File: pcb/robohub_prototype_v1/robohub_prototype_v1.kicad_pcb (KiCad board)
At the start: 10 copper layers, 102 parts, among them J21 Barrel_Jack_Switch_Pin3Ring, J51 USB_A, J52 USB_A, J71 USB_A, U1 ATSAMA5D27C, U21 LM3880, U22 TPS564242DRL, U23 TPS564242DRL, U24 TPS564242DRL, U25 TPS564242DRL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

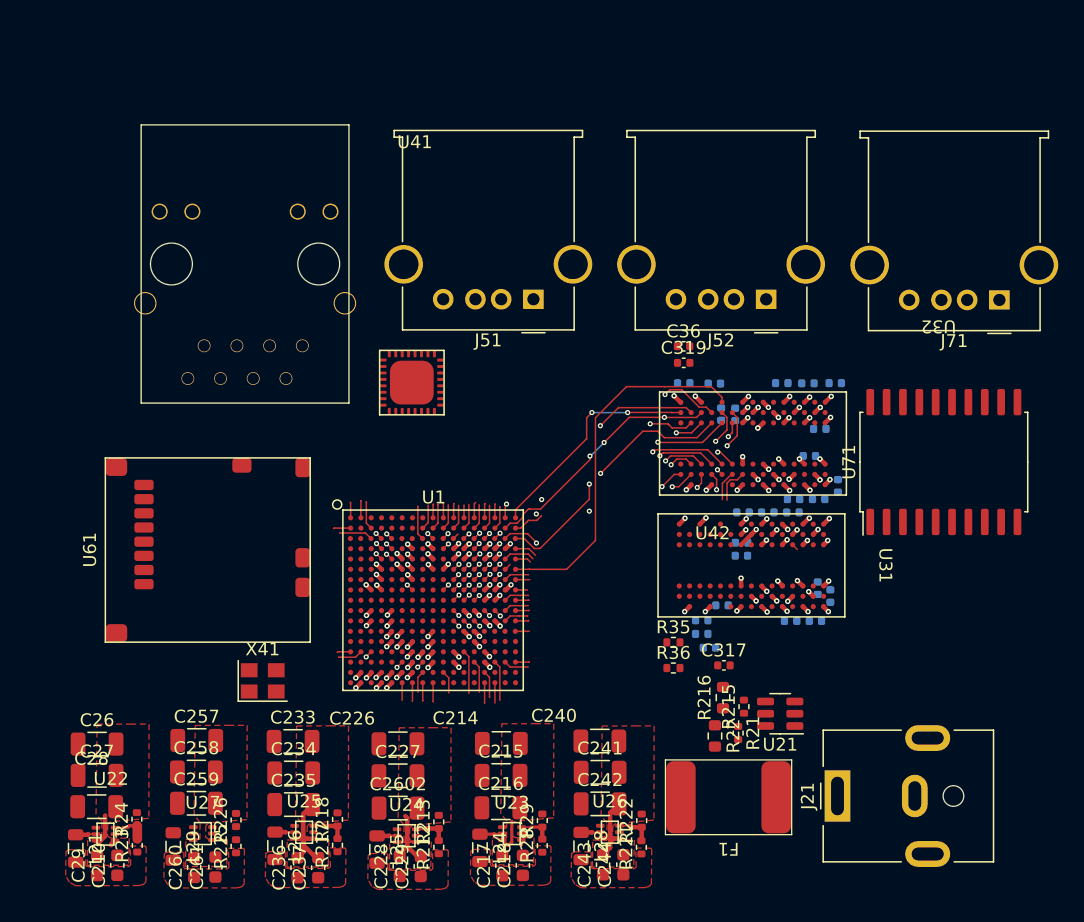
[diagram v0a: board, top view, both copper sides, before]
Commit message: Update schematic for byte swap; change ddr2 layout; begin reroute of ddr2
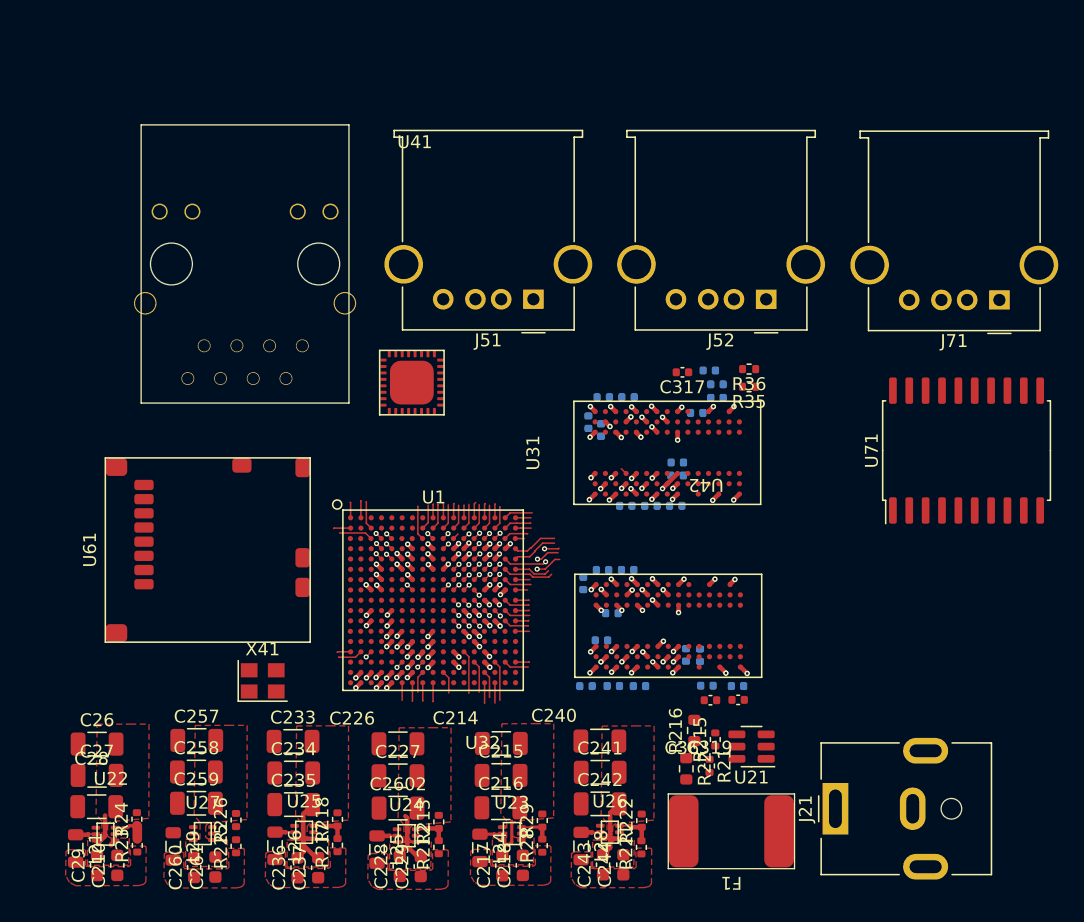
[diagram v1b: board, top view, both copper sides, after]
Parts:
- moved C314 30.4 mm to (133.7, 101.4), turned to 180 degrees
- moved C315 27.9 mm to (135.8, 101.4), turned to 0 degrees
- moved C36 27.5 mm to (143.4, 102.5), turned to 180 degrees
- moved C319 26.5 mm to (145.5, 102.5), turned to 180 degrees
- moved C316 26.0 mm to (137.9, 101.4), turned to 180 degrees
- moved C321 23.9 mm to (135.1, 79.0), turned to 0 degrees
- moved R36 23.9 mm to (146.4, 76.8), turned to 180 degrees
- moved C318 23.9 mm to (145.5, 101.4), turned to 180 degrees
- moved C311 23.6 mm to (134.9, 97.8), turned to 180 degrees
- moved C35 23.5 mm to (143.1, 101.3), turned to 0 degrees
- moved C327 23.1 mm to (133.9, 80.9), turned to -90 degrees
- moved C317 23.0 mm to (141.2, 77.0), turned to 180 degrees
- moved C37 21.5 mm to (143.3, 76.9), turned to 180 degrees
- moved C326 21.5 mm to (137.0, 79.0), turned to 180 degrees
- moved C322 21.2 mm to (133.5, 93.4), turned to 90 degrees
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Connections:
- net VCC_3_3_A renamed VDDBU
- U31 pad A8: /DDR2_3/DDR_DQS1- -> /DDR2_3/DDR_DQS2-
- U31 pad B1: /DDR2_3/DDR_D14 -> /DDR2_3/DDR_D22
- U31 pad B3: /DDR2_3/DDR_DQM1 -> /DDR2_3/DDR_DQM2
- U31 pad B7: /DDR2_3/DDR_DQS1+ -> /DDR2_3/DDR_DQS2+
- U31 pad B9: /DDR2_3/DDR_D15 -> /DDR2_3/DDR_D23
- U31 pad C2: /DDR2_3/DDR_D9 -> /DDR2_3/DDR_D17
- U31 pad C8: /DDR2_3/DDR_D8 -> /DDR2_3/DDR_D16
- U31 pad D1: /DDR2_3/DDR_D12 -> /DDR2_3/DDR_D20
- U31 pad D3: /DDR2_3/DDR_D11 -> /DDR2_3/DDR_D19
- U31 pad D7: /DDR2_3/DDR_D10 -> /DDR2_3/DDR_D18
- U31 pad D9: /DDR2_3/DDR_D13 -> /DDR2_3/DDR_D21
- U32 pad E8: /DDR2_3/DDR_DQS2- -> /DDR2_3/DDR_DQS1-
- U32 pad F1: /DDR2_3/DDR_D22 -> /DDR2_3/DDR_D14
- U32 pad F3: /DDR2_3/DDR_DQM2 -> /DDR2_3/DDR_DQM1
- U32 pad F7: /DDR2_3/DDR_DQS2+ -> /DDR2_3/DDR_DQS1+
- U32 pad F9: /DDR2_3/DDR_D23 -> /DDR2_3/DDR_D15
- U32 pad G2: /DDR2_3/DDR_D17 -> /DDR2_3/DDR_D9
- U32 pad G8: /DDR2_3/DDR_D16 -> /DDR2_3/DDR_D8
- U32 pad H1: /DDR2_3/DDR_D20 -> /DDR2_3/DDR_D12
- U32 pad H3: /DDR2_3/DDR_D19 -> /DDR2_3/DDR_D11
- U32 pad H7: /DDR2_3/DDR_D18 -> /DDR2_3/DDR_D10
- U32 pad H9: /DDR2_3/DDR_D21 -> /DDR2_3/DDR_D13
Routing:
- net /DDR2_3/DDR_BA2: track 28.2 -> 2.82 mm
- net /DDR2_3/DDR_RAS: track 26.7 -> 6.35 mm, vias 3 -> 1
- net /DDR2_3/DDR_CS: track 26.4 -> 6.37 mm, vias 2 -> 1
- net /DDR2_3/DDR_A1: track 20.7 -> 0.70 mm, vias 2 -> 0
- net /DDR2_3/DDR_A10: track 22.4 -> 3.55 mm, vias 2 -> 1
- net /DDR2_3/DDR_A5: track 23.5 -> 5.43 mm, vias 2 -> 1
- net /DDR2_3/DDR_A4: track 20.0 -> 1.91 mm, vias 2 -> 0
- net /DDR2_3/DDR_A0: track 25.1 -> 7.89 mm
- net /DDR2_3/DDR_A3: track 19.2 -> 2.14 mm, vias 3 -> 0
- net /DDR2_3/DDR_A12: track 17.6 -> 1.19 mm, vias 2 -> 0
- net /DDR2_3/DDR_A8: track 21.0 -> 4.72 mm, vias 2 -> 1
- net /DDR2_3/DDR_A7: track 25.5 -> 9.23 mm
- net /DDR2_3/DDR_A11: track 18.2 -> 2.25 mm, vias 4 -> 0
- net /DDR2_3/DDR_A9: track 21.2 -> 5.41 mm, vias 2 -> 1
- net /DDR2_3/DDR_A13: track 23.3 -> 8.91 mm
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
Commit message: Moved some stuff around, tried a route
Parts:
- moved C310 5.03 mm to (133.7, 87.1)
- moved C312 5.03 mm to (131.8, 87.1)
- moved C320 5.03 mm to (138.9, 78.7)
- moved C331 5.03 mm to (135.8, 83.7)
- moved C37 5.03 mm to (138.3, 76.6)
- moved C39 5.03 mm to (135.7, 87.1)
- moved R35 5.03 mm to (141.3, 77.8)
- moved R36 5.03 mm to (141.3, 76.5)
- moved U31 5.03 mm to (135.0, 83.0)
- moved C321 5.03 mm to (130.0, 78.7)
- moved C325 5.03 mm to (129.9, 81.2)
- moved C327 5.03 mm to (128.9, 80.6)
- moved C328 5.03 mm to (137.3, 79.9)
- moved C330 5.03 mm to (135.8, 84.7)
- moved C38 5.03 mm to (138.9, 77.7)
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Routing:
- net /DDR2_3/DDR_A12: track 1.19 -> 15.9 mm
- net /DDR2_3/DDR_A7: track 9.23 -> 0.90 mm, vias 2 -> 1
- net /DDR2_3/DDR_A13: track 8.91 -> 0.57 mm, vias 2 -> 1
- net /DDR2_3/DDR_A0: track 7.89 -> 0.58 mm, vias 2 -> 1
- net /DDR2_3/DDR_CKE: track 3.94 -> 0.00 mm
- net /DDR2_3/DDR_CLK+: track 3.57 -> 0.00 mm
- net /DDR2_3/DDR_CLK-: track 3.58 -> 0.15 mm
- net /DDR2_3/DDR_BA2: track 2.82 -> 0.01 mm
- net /DDR2_3/DDR_A11: track 2.25 -> 0.00 mm
- net /DDR2_3/DDR_A3: track 2.14 -> 0.67 mm
- net /DDR2_3/DDR_A2: track 1.21 -> 0.00 mm
- net Net-(U1E-DDR_RESETN): track 3.37 -> 2.81 mm, vias 1 -> 0
- net VCC_1_8_DDR: vias 39 -> 38

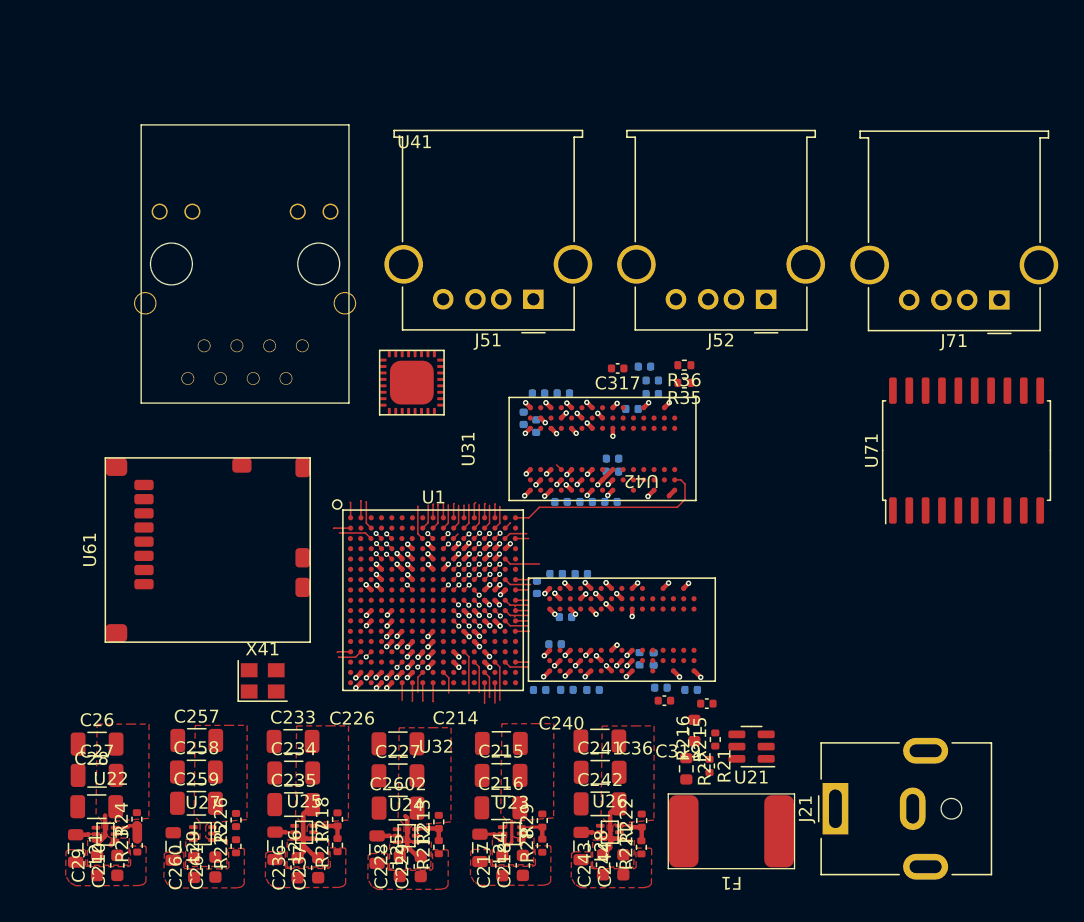
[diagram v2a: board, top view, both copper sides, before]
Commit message: Update PCB route to match example design
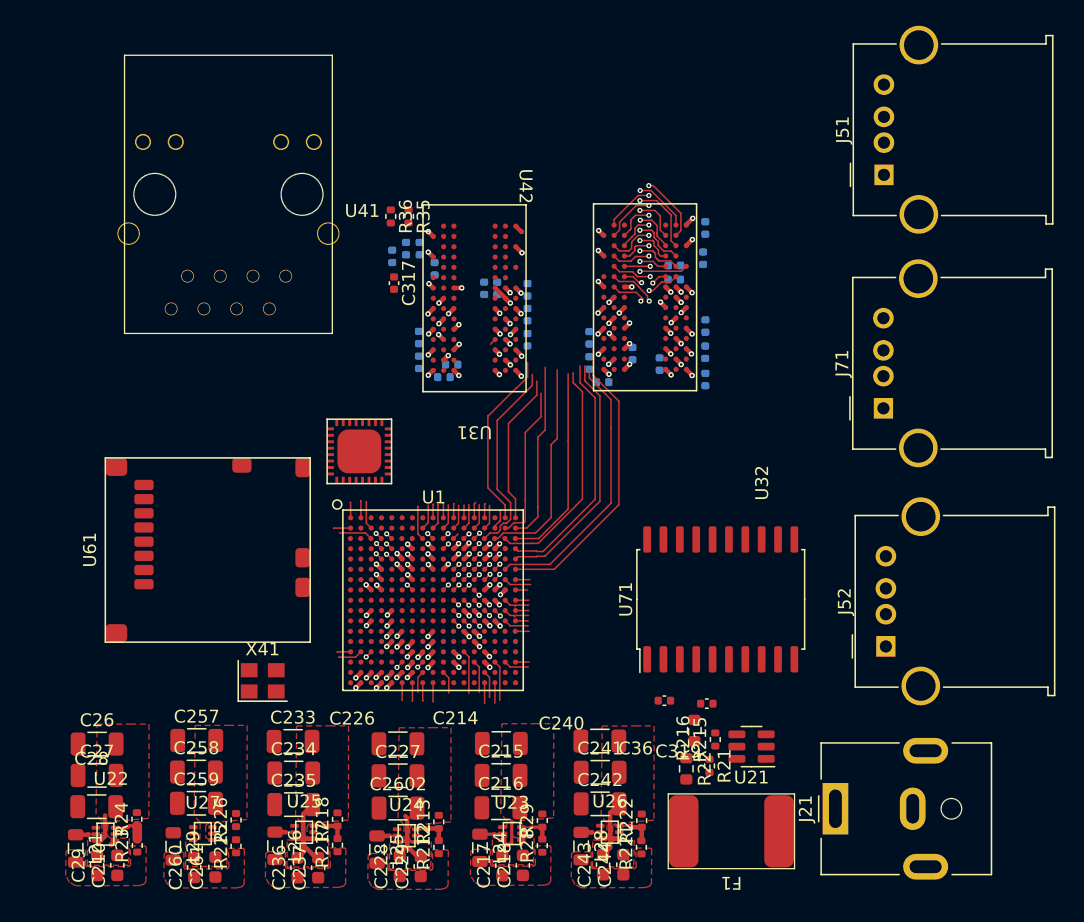
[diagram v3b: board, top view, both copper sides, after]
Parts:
- moved C318 35.9 mm to (143.0, 65.8), turned to -90 degrees
- moved C35 33.5 mm to (142.8, 68.2), turned to 90 degrees
- moved C34 30.6 mm to (140.6, 68.7), turned to 180 degrees
- moved C316 29.6 mm to (143.0, 73.4), turned to -90 degrees
- moved C33 29.6 mm to (140.6, 69.8), turned to 180 degrees
- moved J51 28.9 mm to (156.8, 61.7), turned to 90 degrees
- moved J52 28.5 mm to (157.0, 98.3), turned to 90 degrees
- moved C315 28.3 mm to (143.0, 75.5), turned to 90 degrees
- moved C314 27.3 mm to (143.0, 77.6), turned to -90 degrees
- moved U32 25.9 mm to (138.3, 71.2), turned to 180 degrees
- moved R36 25.5 mm to (118.6, 64.9), turned to -90 degrees
- moved R35 25.0 mm to (119.9, 64.9), turned to -90 degrees
- moved C311 23.2 mm to (139.4, 76.4), turned to -90 degrees
- moved U71 22.3 mm to (144.2, 94.7)
- moved C38 21.7 mm to (119.8, 67.4), turned to 90 degrees
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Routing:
- net /DDR2_3/DDR_BA2: track 0.01 -> 26.8 mm, vias 0 -> 1
- net /DDR2_3/DDR_CKE: track 0.00 -> 23.9 mm, vias 0 -> 1
- net /DDR2_3/DDR_CLK-: track 0.15 -> 22.6 mm, vias 0 -> 1
- net /DDR2_3/DDR_CLK+: track 0.00 -> 22.2 mm, vias 0 -> 1
- net /DDR2_3/DDR_A10: track 3.55 -> 23.7 mm
- net /DDR2_3/DDR_A4: track 1.86 -> 21.4 mm, vias 0 -> 1
- net /DDR2_3/DDR_A8: track 4.72 -> 23.8 mm
- net /DDR2_3/DDR_A1: track 1.07 -> 18.4 mm, vias 0 -> 1
- net /DDR2_3/DDR_A3: track 0.67 -> 17.7 mm, vias 0 -> 1
- net /DDR2_3/DDR_A11: track 0.00 -> 16.9 mm, vias 0 -> 1
- net /DDR2_3/DDR_A2: track 0.00 -> 16.3 mm, vias 0 -> 1
- net /DDR2_3/DDR_A7: track 0.90 -> 6.15 mm, vias 1 -> 2
- net /DDR2_3/DDR_A13: track 0.57 -> 4.48 mm, vias 1 -> 2
- net /DDR2_3/DDR_BA0: track 7.08 -> 10.6 mm, vias 1 -> 2
- net /DDR2_3/DDR_A9: track 5.41 -> 8.86 mm, vias 1 -> 2
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
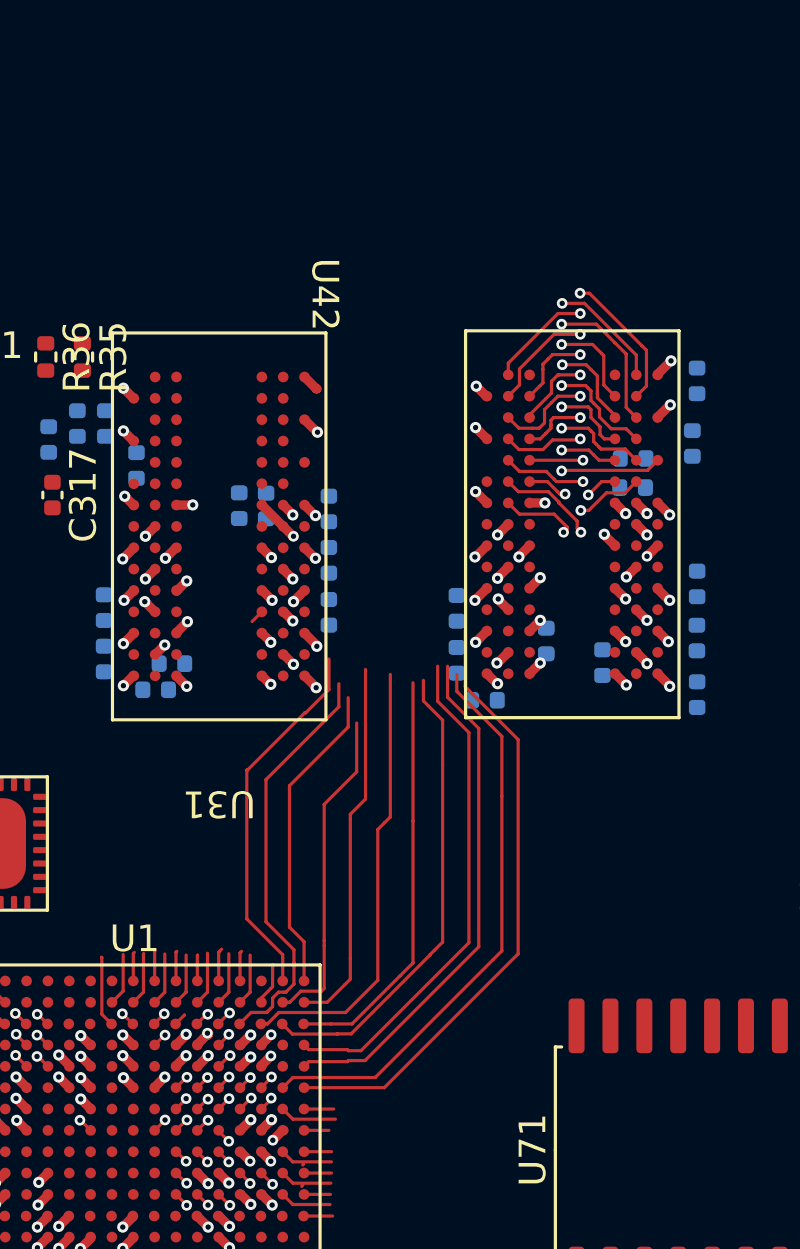
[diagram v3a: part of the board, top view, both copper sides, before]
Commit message: Update PCB routing of DDR2
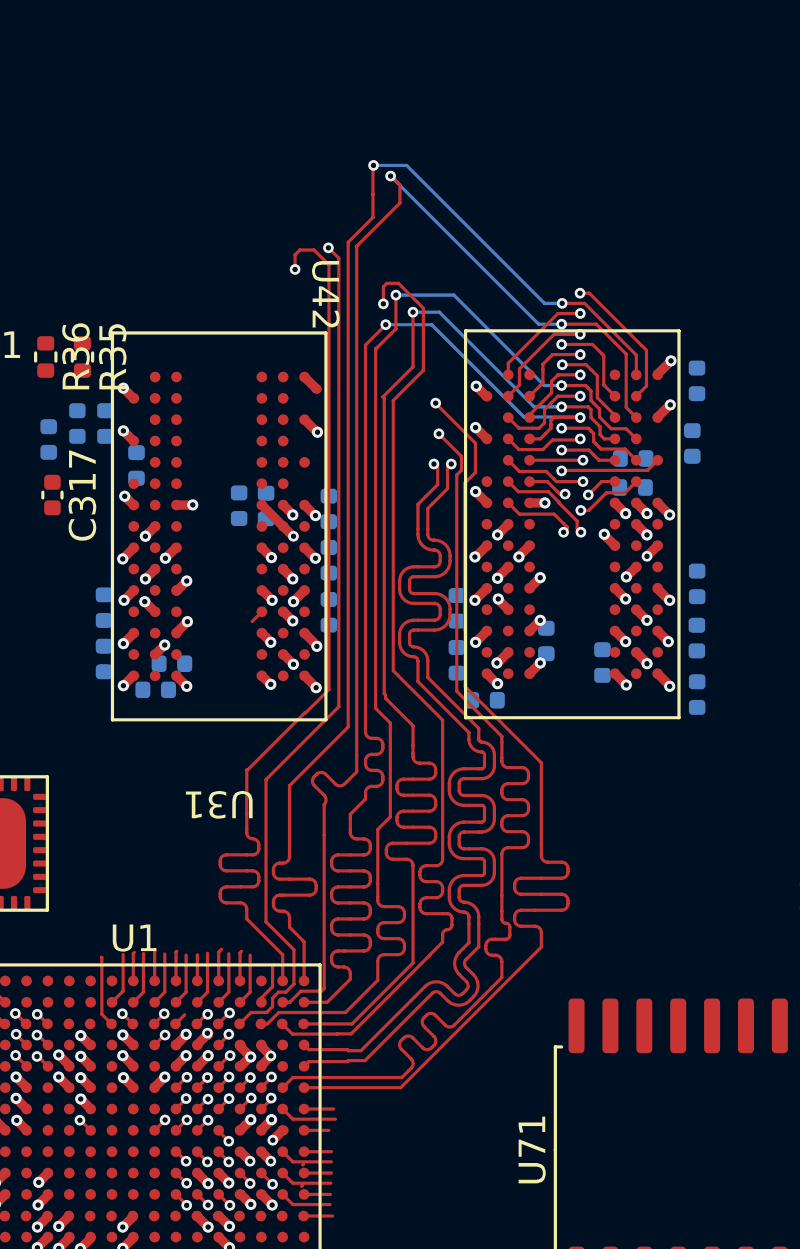
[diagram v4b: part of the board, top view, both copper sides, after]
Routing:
- net /DDR2_3/DDR_A11: track 16.9 -> 50.5 mm, vias 1 -> 2
- net /DDR2_3/DDR_A2: track 16.3 -> 49.6 mm, vias 1 -> 2
- net /DDR2_3/DDR_A12: track 16.1 -> 49.1 mm, vias 1 -> 2
- net /DDR2_3/DDR_A3: track 17.7 -> 49.3 mm, vias 1 -> 2
- net /DDR2_3/DDR_A1: track 18.4 -> 48.2 mm, vias 1 -> 2
- net /DDR2_3/DDR_A4: track 21.4 -> 50.8 mm, vias 1 -> 2
- net /DDR2_3/DDR_CLK-: track 22.6 -> 49.6 mm, vias 1 -> 2
- net /DDR2_3/DDR_CLK+: track 22.2 -> 47.8 mm, vias 1 -> 2
- net /DDR2_3/DDR_CKE: track 23.9 -> 49.5 mm, vias 1 -> 2
- net /DDR2_3/DDR_A8: track 23.8 -> 47.0 mm, vias 1 -> 2
- net /DDR2_3/DDR_BA2: track 26.8 -> 49.9 mm, vias 1 -> 2
- net /DDR2_3/DDR_A10: track 23.7 -> 46.2 mm, vias 1 -> 2
- net /DDR2_3/DDR_BA1: track 9.28 -> 2.74 mm
- net /DDR2_3/DDR_BA0: track 10.6 -> 4.07 mm
- net /DDR2_3/DDR_CAS: track 9.00 -> 2.60 mm
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
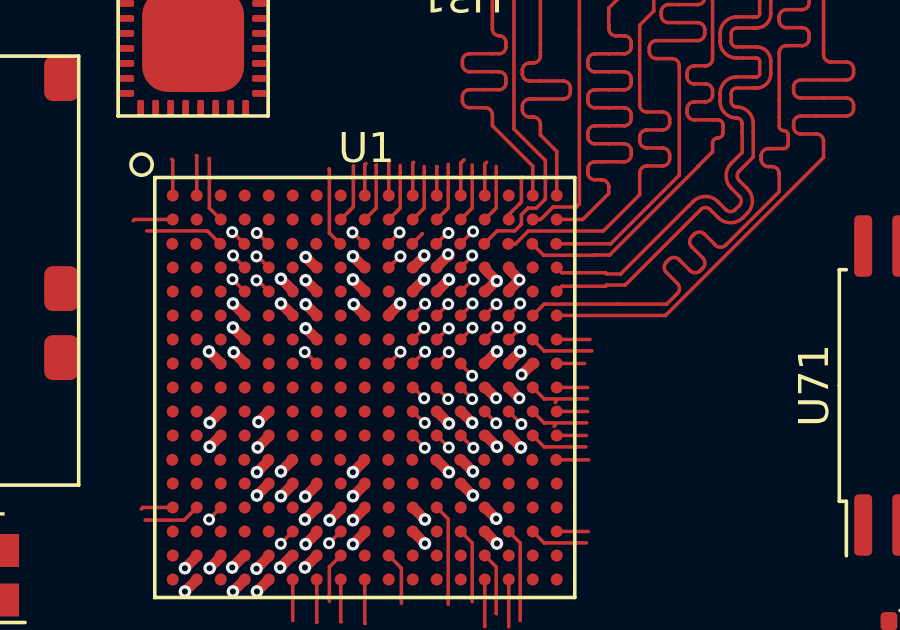
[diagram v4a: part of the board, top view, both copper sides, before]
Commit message: Started routing inner layer ddr2
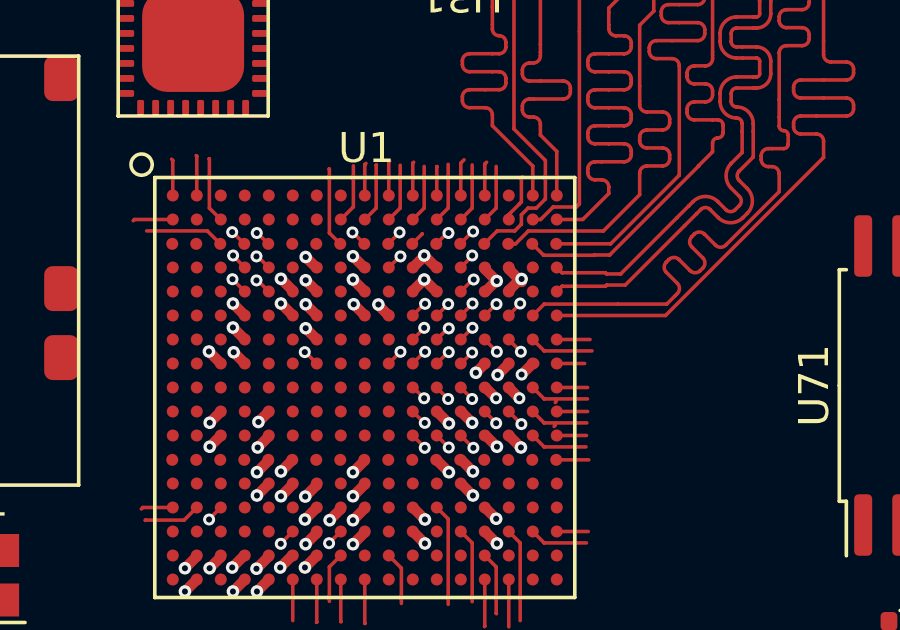
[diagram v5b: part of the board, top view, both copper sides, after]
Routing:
- net /DDR2_3/DDR_BA0: track 4.07 -> 15.3 mm
- net /DDR2_3/DDR_BA1: track 2.74 -> 13.8 mm
- net /DDR2_3/DDR_A5: track 3.93 -> 14.5 mm
- net /DDR2_3/DDR_WE: track 1.86 -> 9.95 mm
- net /DDR2_3/DDR_CS: track 3.78 -> 11.6 mm
- net /DDR2_3/DDR_A7: track 6.15 -> 13.7 mm
- net /DDR2_3/DDR_RAS: track 2.17 -> 9.58 mm
- net /DDR2_3/DDR_CAS: track 2.60 -> 9.98 mm
- net /DDR2_3/DDR_A6: track 3.47 -> 10.7 mm
- net /DDR2_3/DDR_A0: track 3.61 -> 10.0 mm
- net /DDR2_3/DDR_A13: track 4.48 -> 10.6 mm
- net /DDR2_3/DDR_A9: track 7.09 -> 8.54 mm
- net GND: track 62.7 -> 62.6 mm, vias 59 -> 58
- net VCC_1_8_DDR: track 24.1 -> 24.2 mm, vias 37 -> 36
